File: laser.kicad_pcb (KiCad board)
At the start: 4 copper layers, 90.2 x 50.9 mm, 129 parts, among them IC201 ADM7172ACPZ-4.2-R7, IC202 LT1716CS5#TRPBF, IC203 ADM7154ARDZ-3.3-R7, IC204 IRF9358PBF, IC601 ATMEGA328P-AU, IC602 FT232RL-TUBE, IC701 MAX6126AASA25+, IC801 ADS122C04IPWR, J601 M20-9980345, J602 USB_Connector, Q401 RSR030N06TL, U101 281698-3, U201 LM4040EIM3X-2.5_NOPB, U301 OPA569AIDWPR, U302 OPA569AIDWPR, U401 ADA4528-2ACPZ-RL, U402 782853152_WE-CBA_08, U501 ADA4528-2ACPZ-RL, U502 ADA4528-2ACPZ-RL, U801 MAX5217GUA+, U802 MAX5217GUA+, Y601 ECS-160-16-33B-CKM-TR

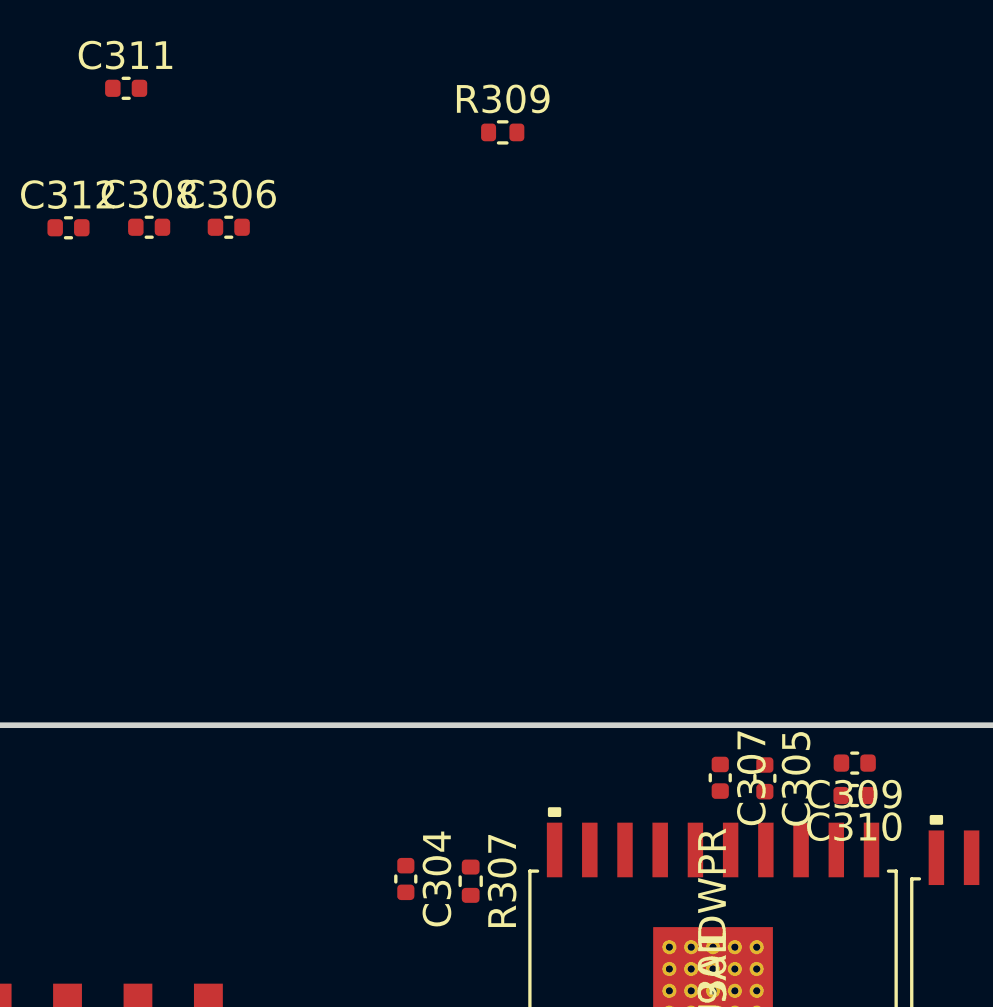
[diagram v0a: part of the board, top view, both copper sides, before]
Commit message: reload C305 and C306
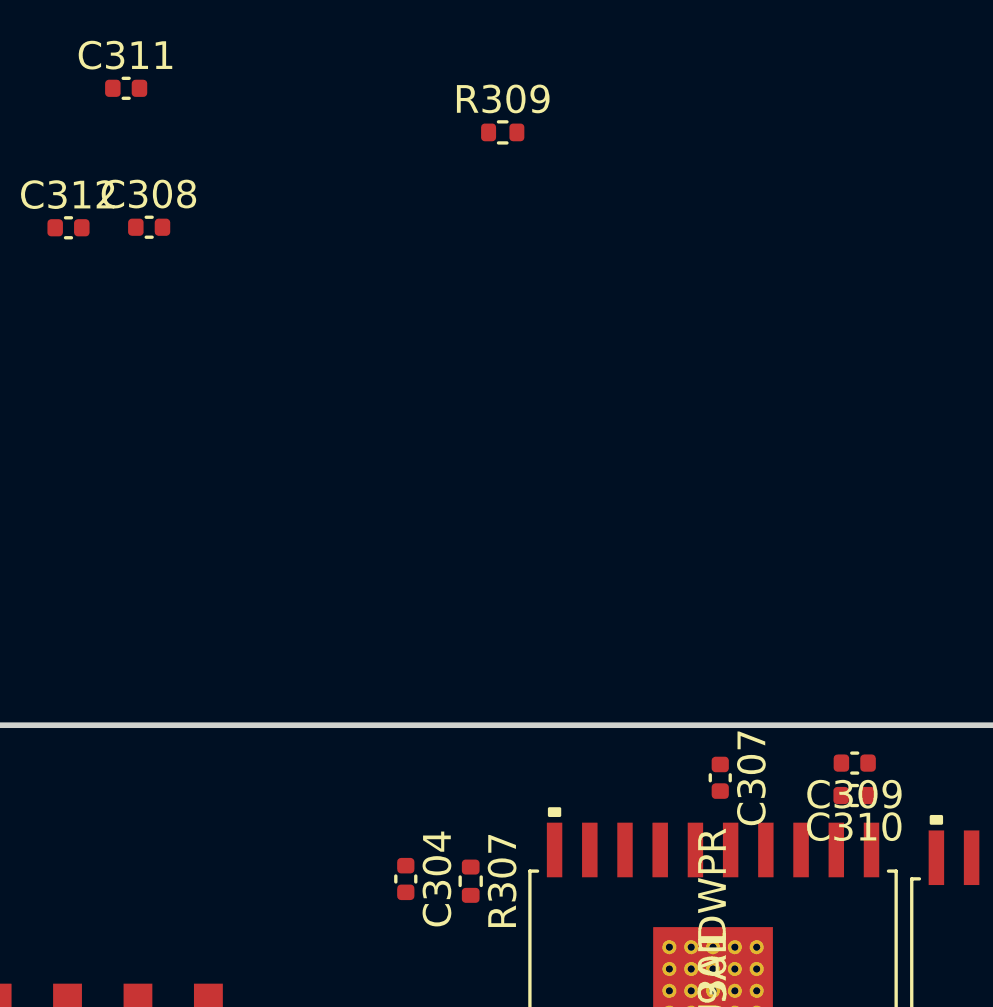
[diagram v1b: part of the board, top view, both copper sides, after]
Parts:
- removed the C305 at (165.7, 83.2)
- removed the C306 at (146.4, 63.4)

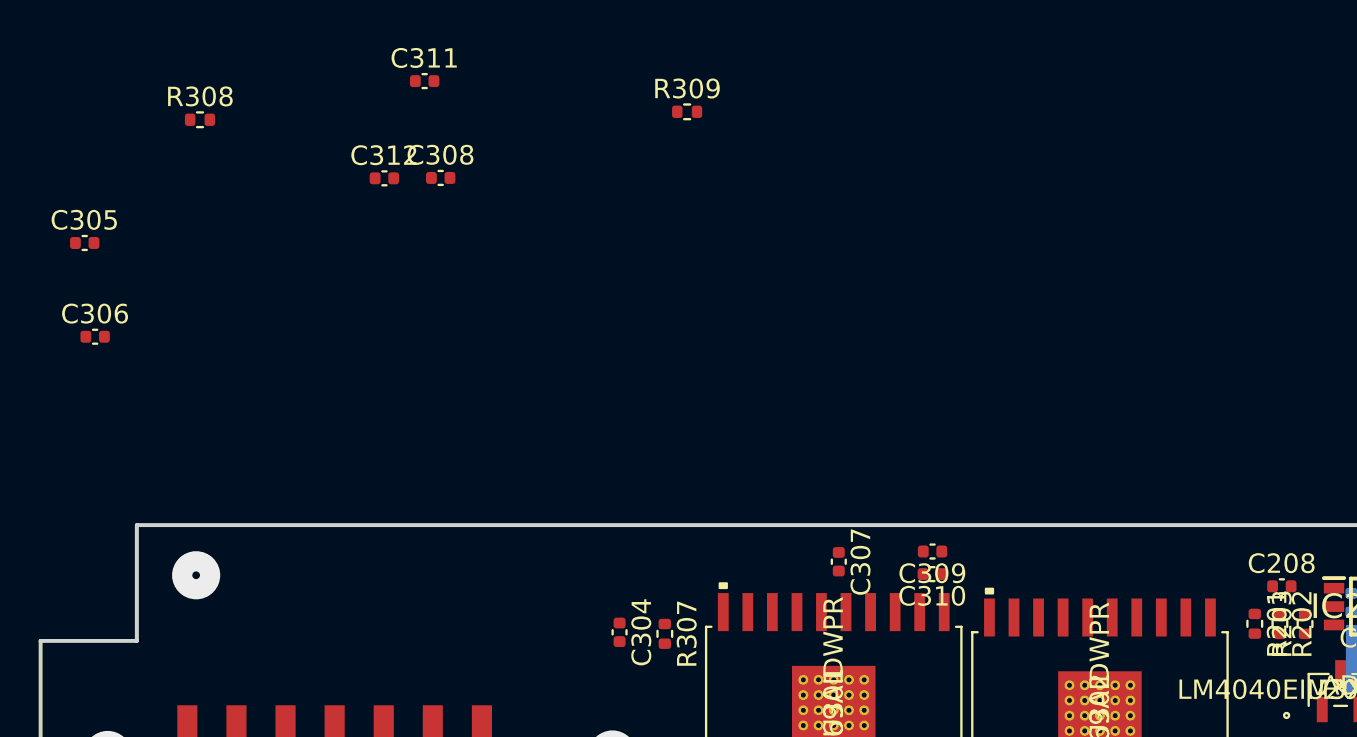
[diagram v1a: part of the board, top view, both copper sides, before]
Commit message: finished positioning opamps
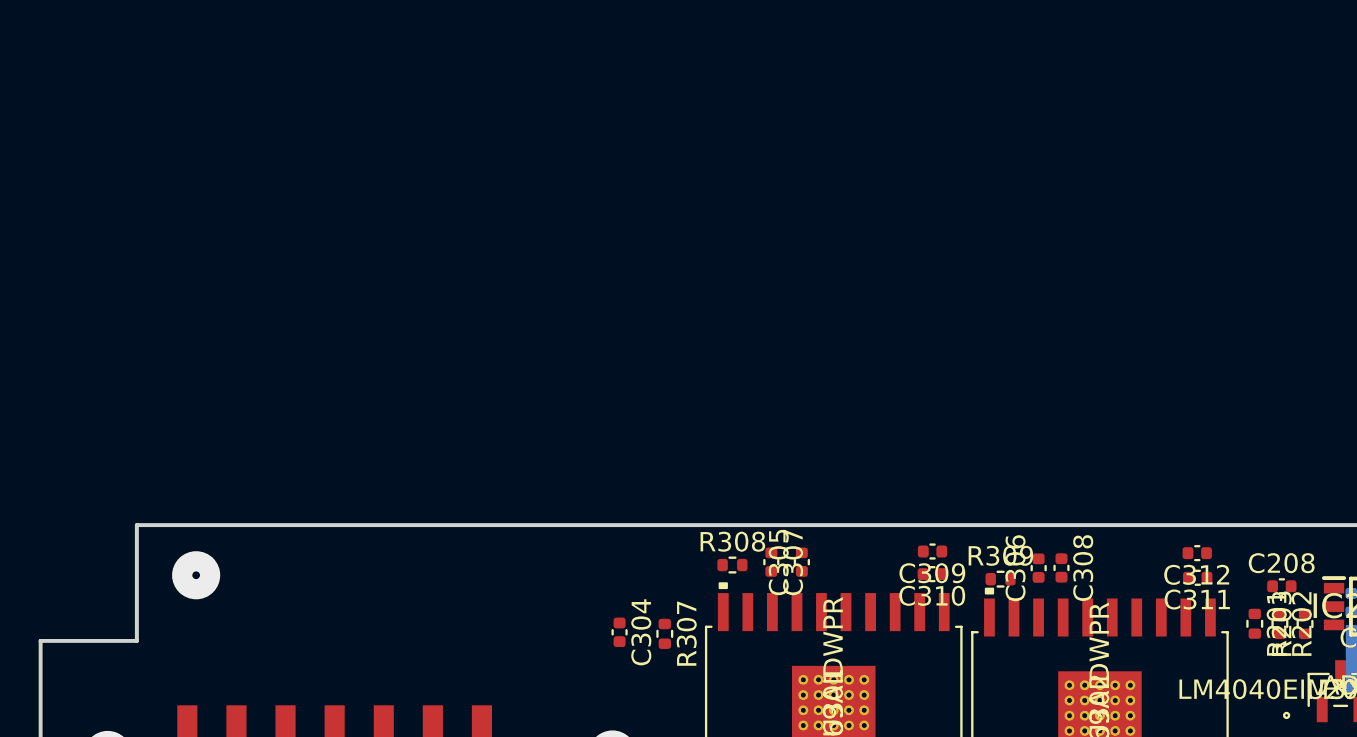
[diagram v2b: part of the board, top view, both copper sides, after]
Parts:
- moved C306 50.3 mm to (174.4, 83.6), turned to 90 degrees
- moved C311 47.5 mm to (182.7, 84.1), turned to 180 degrees
- moved C312 46.3 mm to (182.6, 82.8), turned to 180 degrees
- moved C305 40.6 mm to (162.2, 83.2), turned to 90 degrees
- moved C308 37.9 mm to (175.6, 83.5), turned to 270 degrees
- moved R308 35.9 mm to (158.6, 83.4)
- moved R309 29.1 mm to (172.4, 84.1)
- moved C307 3.49 mm to (160.6, 83.2)

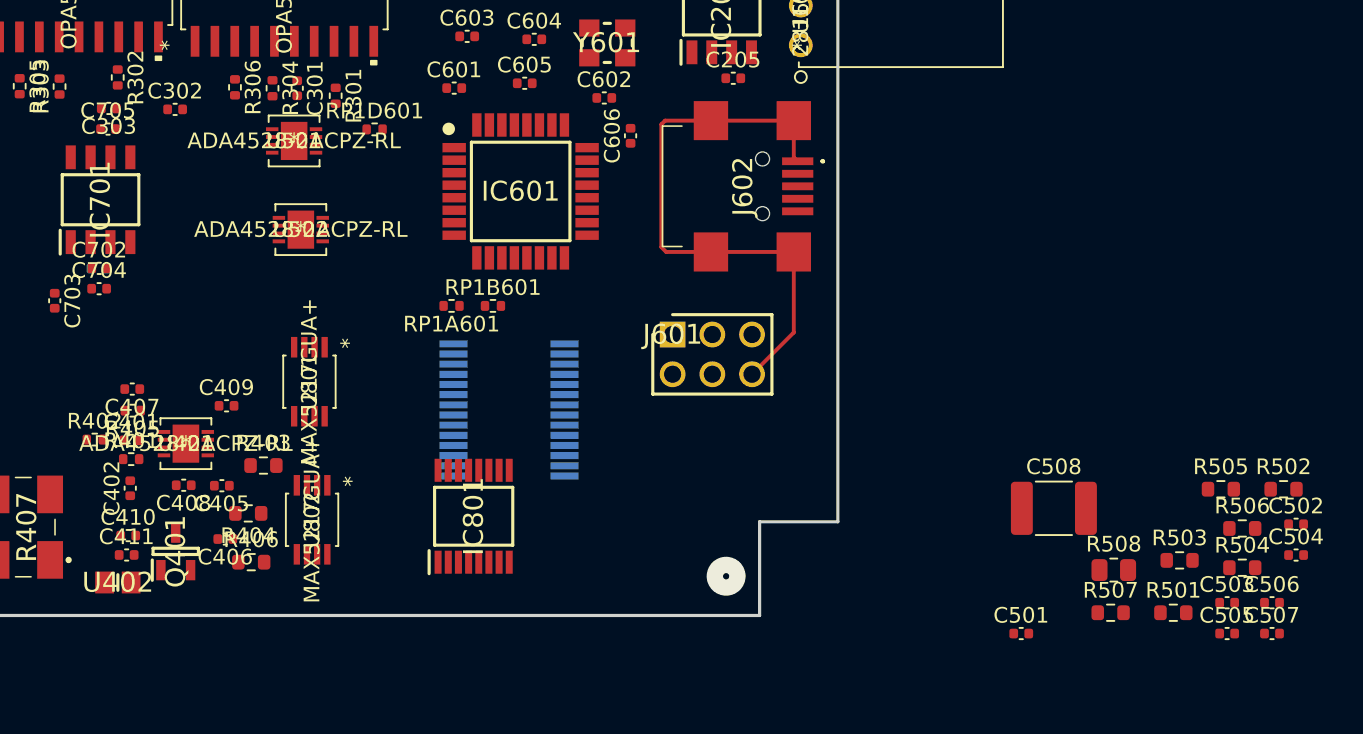
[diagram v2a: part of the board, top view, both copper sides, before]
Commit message: finish placing thermalcontrol
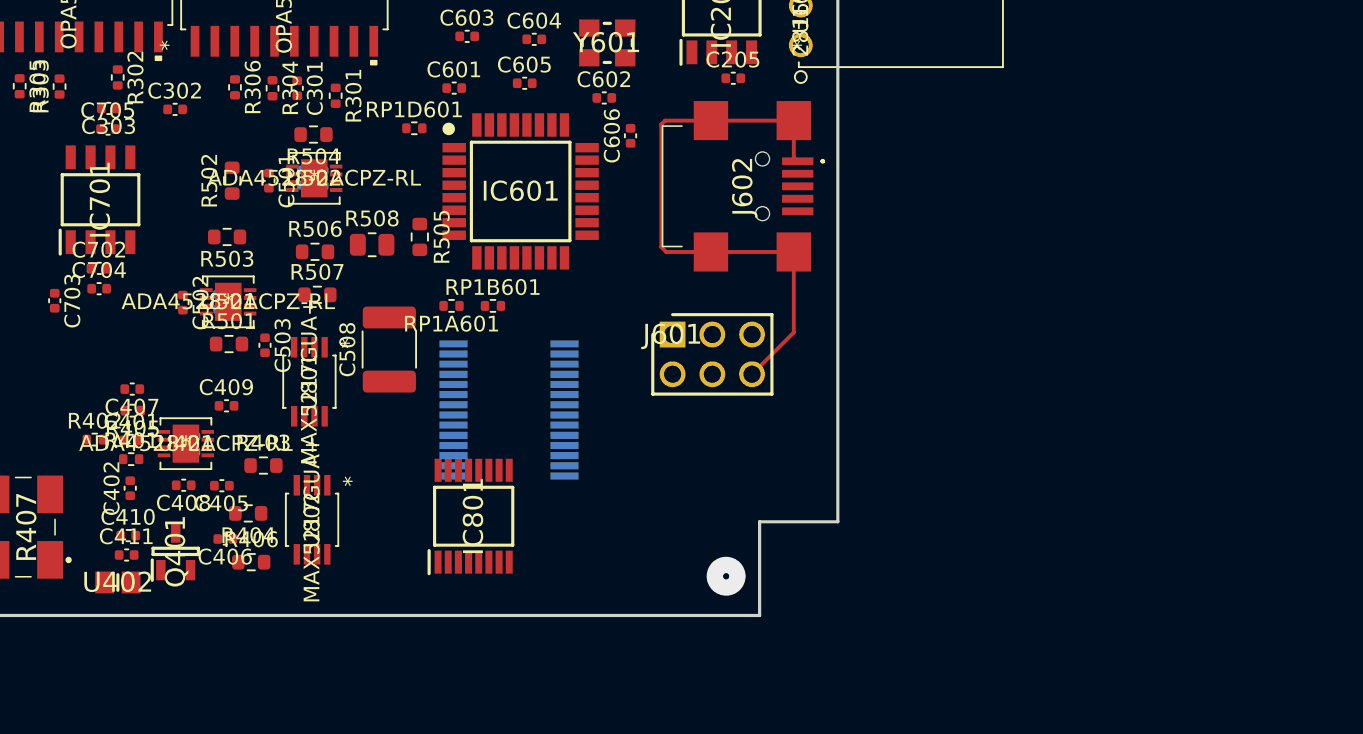
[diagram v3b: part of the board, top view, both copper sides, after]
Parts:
- C504, C505, C506, C507: moved to B.Cu
- moved C502 72.6 mm to (171.1, 112.2), turned to 270 degrees
- moved C504 70.8 mm to (171.9, 121.2), turned to 270 degrees
- moved R502 70.1 mm to (174.2, 104.4), turned to 90 degrees
- moved C505 67.9 mm to (173.3, 112.2), turned to 270 degrees
- moved C506 67.8 mm to (178.7, 104.2), turned to 270 degrees
- moved C507 67.3 mm to (180.1, 104.2), turned to 270 degrees
- moved R504 65.5 mm to (179.4, 101.5), turned to 180 degrees
- moved R503 64.3 mm to (173.9, 108.0), turned to 180 degrees
- moved C503 63.7 mm to (176.3, 114.9), turned to 270 degrees
- moved R501 62.8 mm to (174.1, 114.8)
- moved R506 61.9 mm to (179.6, 109.0)
- moved C501 56.2 mm to (176.6, 104.4), turned to 270 degrees
- moved R507 54.7 mm to (179.7, 111.7)
- moved R505 53.7 mm to (186.2, 108.0), turned to 270 degrees
- moved R508 51.8 mm to (183.2, 108.5)
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
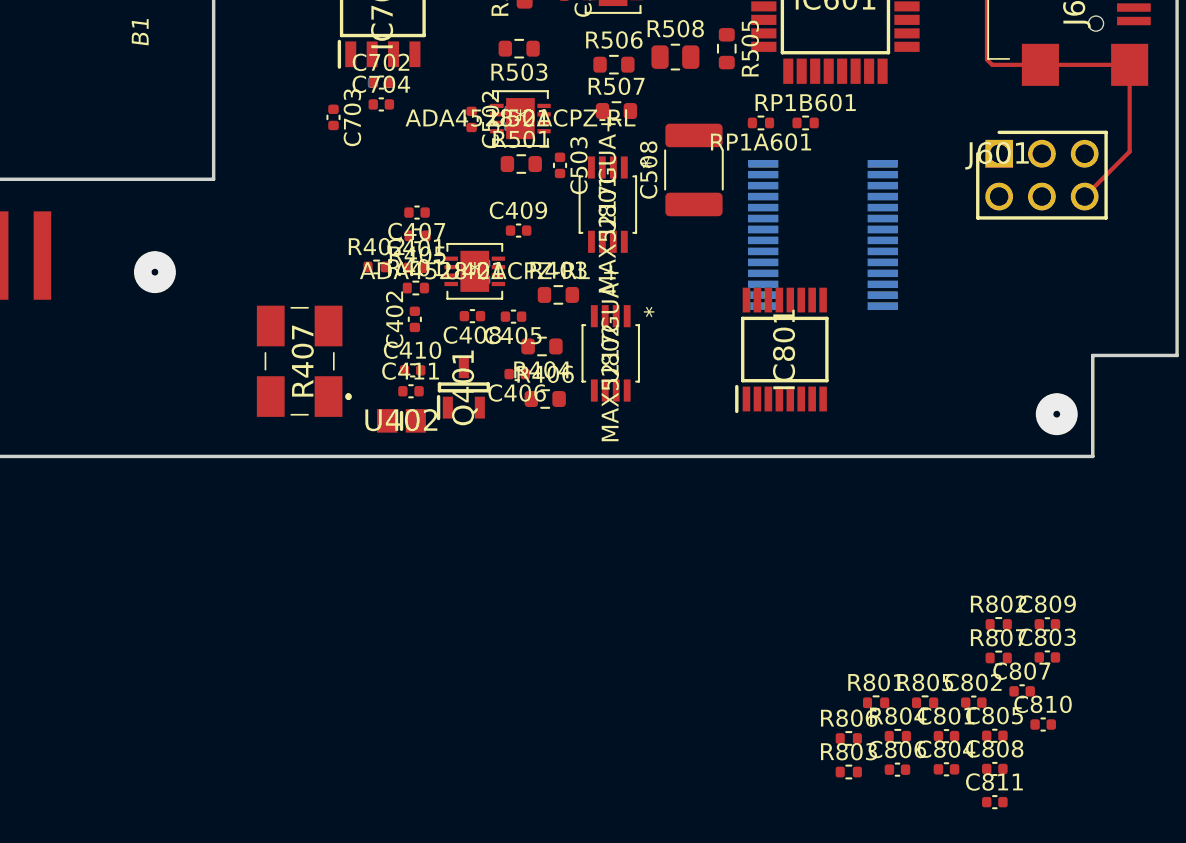
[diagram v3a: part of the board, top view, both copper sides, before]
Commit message: component placement completed
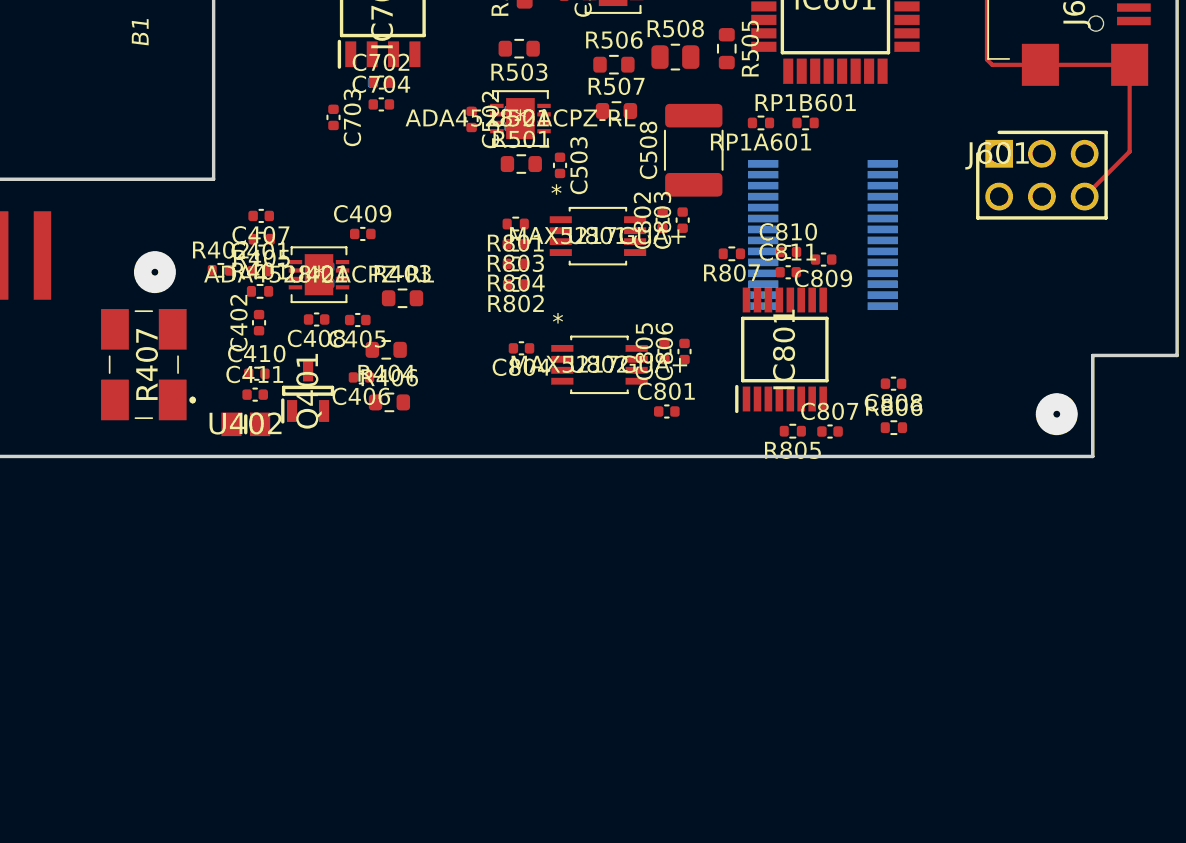
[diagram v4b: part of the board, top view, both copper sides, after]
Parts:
- moved R803 37.1 mm to (173.7, 119.6), turned to 180 degrees
- moved R804 36.1 mm to (173.7, 120.8), turned to 180 degrees
- moved R801 35.6 mm to (173.7, 118.4), turned to 180 degrees
- moved C804 35.5 mm to (174.1, 125.8), turned to 180 degrees
- moved R802 35.1 mm to (173.7, 122.0), turned to 180 degrees
- moved C802 34.1 mm to (182.4, 118.2), turned to 90 degrees
- moved C803 33.8 mm to (183.6, 118.2), turned to 90 degrees
- moved C811 33.8 mm to (189.9, 121.3)
- moved C810 31.9 mm to (189.9, 120.1)
- moved C805 30.1 mm to (182.6, 126.0), turned to 90 degrees
- moved R807 28.8 mm to (186.6, 120.2), turned to 180 degrees
- moved C806 27.9 mm to (183.7, 126.0), turned to 90 degrees
- moved C801 25.4 mm to (182.7, 129.5)
- moved C809 25.4 mm to (192.0, 120.5), turned to 180 degrees
- moved C808 23.7 mm to (196.2, 127.9), turned to 180 degrees
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
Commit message: final edits since Monday
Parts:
- moved C408 1.38 mm to (160.6, 124.5)
- moved C405 1.08 mm to (163.3, 124.5)
- moved C604 0.64 mm to (192.9, 95.2)
- moved Y601 0.64 mm to (198.2, 95.0)
- moved C502 0.56 mm to (170.6, 112.3)
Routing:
- net GND: track 36.6 -> 73.7 mm, vias 0 -> 18
